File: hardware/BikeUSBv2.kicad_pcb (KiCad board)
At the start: 2 copper layers, 43.6 x 25.5 mm, 53 parts, among them J1 TYPE-C-31-M-16, J2 JST S2B-EH(LF)(SN), SW1 1TS002E-2500-2501-CT, SW2 1TS002E-2500-2501-CT, U1 TPS63020DSJR, U2 ATtiny1616-M, U3 FUSB302B10MPX, U4 HT7550-2, U5 TPS259251

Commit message: remove leftover silkscreen text
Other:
- board text removed: "+ -"
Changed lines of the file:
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@@
     (effects (font (size 1 1) (thickness 0.15)) (justify bottom mirror))
-  )
-  (gr_text "+ -" (at 131 86 90) (layer "B.SilkS")
-    (effects (font (size 1.27 1.27) (thickness 0.15)) (justify top mirror))
   )
   (gr_text "@h3wastooshort\n/BikeUSBv2" (at 153 107) (layer "B.SilkS")

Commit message: slight layout improvment
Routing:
- net /CC_DAC: track 11.0 -> 10.2 mm
- net Net-(JP1-B): track 5.37 -> 4.80 mm

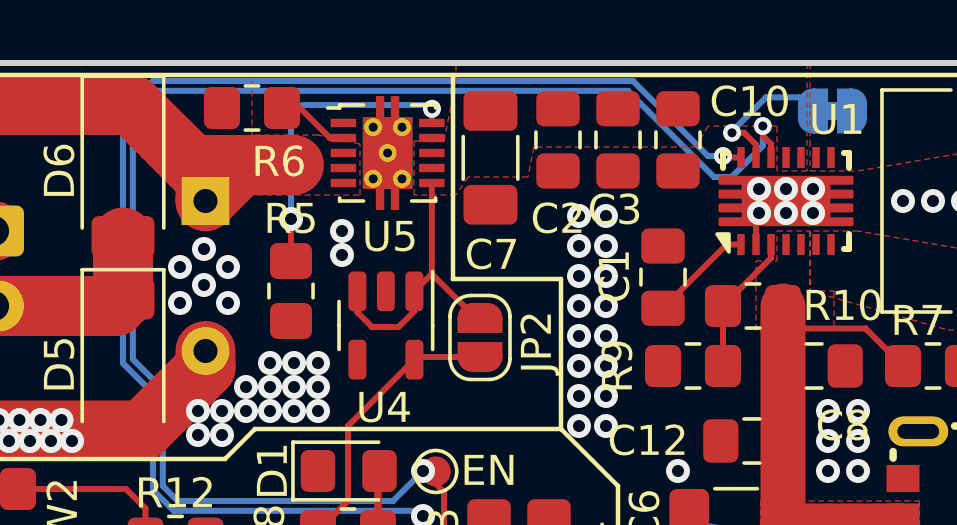
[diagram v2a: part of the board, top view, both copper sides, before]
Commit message: switch eFuse IC in design
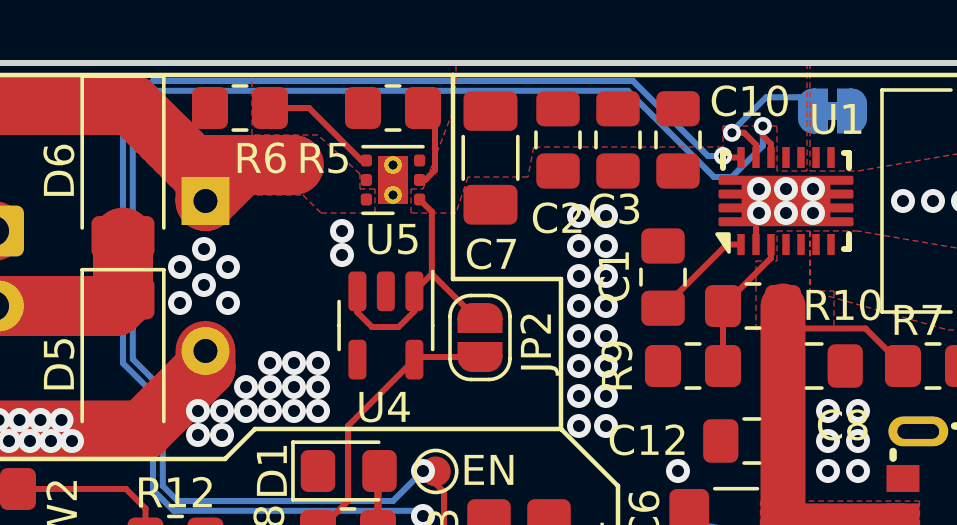
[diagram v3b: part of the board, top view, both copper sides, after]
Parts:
- R5: value 100k -> 33k
- R6: value 1M -> 300k
- U5: value TPS259251 -> TPS25200; footprint Package_SON:VSON-10-1EP_3x3mm_P0.5mm_EP1.65x2.4mm_ThermalVias -> Package_SON:WSON-6-1EP_2x2mm_P0.65mm_EP1x1.6mm_ThermalVias
- moved R5 6.98 mm to (129.5, 83.9), turned to 180 degrees
- moved U5 0.92 mm to (129.5, 86.3), turned to 180 degrees
- moved R6 0.40 mm to (124.4, 83.9)
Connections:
- R6 pad 2: Net-(U5-EN/UVLO) -> Net-(U5-EN)
- U5 pad 1: unconnected-(U5-dV/dT-Pad1) -> +6V
- U5 pad 2: Net-(U5-EN/UVLO) -> Net-(U5-ILIM)
- U5 pad 3: VPP -> unconnected-(U5-FAULT-Pad3)
- U5 pad 4: VPP -> Net-(U5-EN)
- U5 pad 5: VPP -> GND
- U5 pad 6: +6V -> VPP
- U5 pad 7: +6V -> GND
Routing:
- net Net-(U5-ILIM): track 10.2 -> 2.89 mm, vias 2 -> 0
- net Net-(U5-EN): track 0.00 -> 3.54 mm
- net Net-(U5-EN/UVLO): track 2.46 -> 0.00 mm

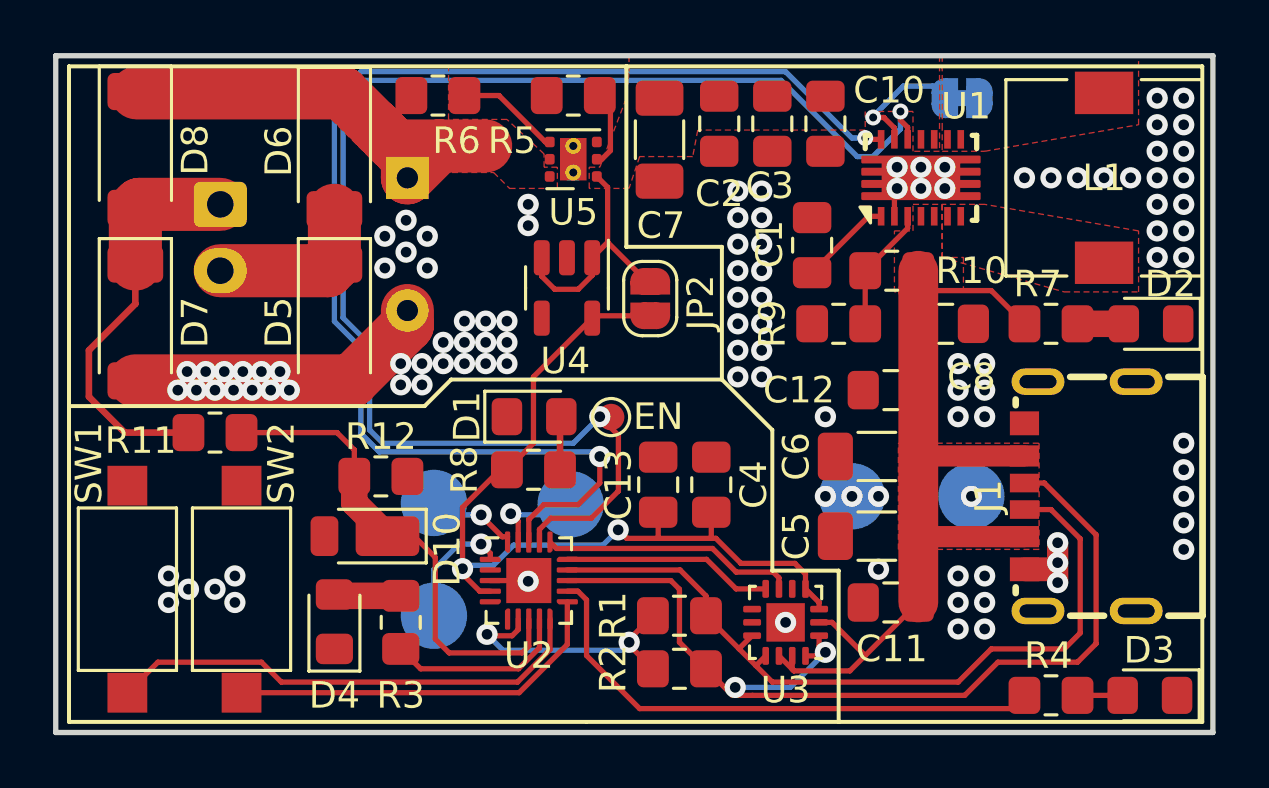
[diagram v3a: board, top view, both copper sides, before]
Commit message: make U4 optional since new U5 clamps to 5V5
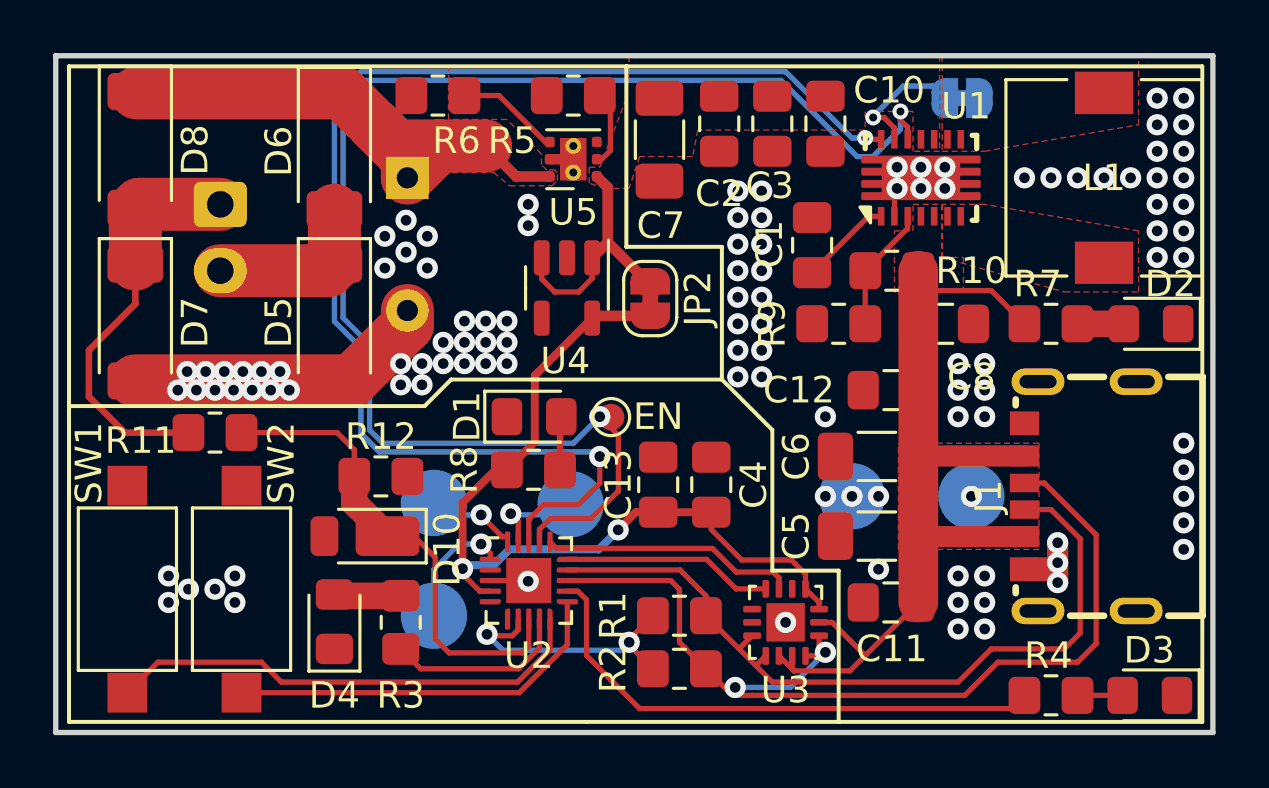
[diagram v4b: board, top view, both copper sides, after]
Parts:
- JP2: footprint Jumper:SolderJumper-2_P1.3mm_Open_RoundedPad1.0x1.5mm -> Jumper:SolderJumper-2_P1.3mm_Bridged_RoundedPad1.0x1.5mm
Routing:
- net VPP: track 18.2 -> 21.1 mm
- net VCC: track 33.1 -> 32.1 mm
- net GND: track 16.7 -> 17.5 mm

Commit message: cleanup
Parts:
- moved C3 1.38 mm to (132.8, 86.9)
- moved R1 0.60 mm to (125.0, 83.9)
- renumbered C9 to C0, C2 to C1, C4 to C10, C5 to C11, C11 to C12, C3 to C2, C7 to C3, C10 to C4, C1 to C5, C8 to C6, C12 to C7, C6 to C8, C13 to C9, JP2 to JP1, JP1 to JP2, R6 to R1, R1 to R10, R2 to R11, R4 to R12, R5 to R2, R10 to R3, R9 to R4, R7 to R5, R11 to R6, R12 to R7, R3 to R9, SW2 to SW1, SW1 to SW2, TP7 to TP1, TP6 to TP2, TP2 to TP3, TP1 to TP4, TP4 to TP5, TP5 to TP6

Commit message: auto cleanup
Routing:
- net Net-(U5-ILIM): track 2.89 -> 2.32 mm
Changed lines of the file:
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@@
   (segment (start 138.7625 103.25) (end 138.7625 103) (width 0.2) (layer "F.Cu") (net 3))
   (segment (start 131.8565 99.6) (end 131.191 100.2655) (width 0.3) (layer "F.Cu") (net 3))
-  (segment (start 130.3 92.2) (end 130.2125 92.2875) (width 0.2) (layer "F.Cu") (net 3))
   (segment (start 138.25 101.928) (end 137.722 101.4) (width 0.2) (layer "F.Cu") (net 3))
   (segment (start 125.975 102.575) (end 125.327 101.927) (width 0.2) (layer "F.Cu") (net 3))
@@
   (segment (start 148.5 105.25) (end 145.5 105.25) (width 0.2) (layer "F.Cu") (net 27))
   (segment (start 149.2 104.55) (end 148.5 105.25) (width 0.2) (layer "F.Cu") (net 27))
-  (segment (start 136.25 106.5) (end 135.5 106.5) (width 0.2) (layer "F.Cu") (net 27))
+  (segment (start 135.5 106.5) (end 144.25 106.5) (width 0.2) (layer "F.Cu") (net 27))
   (segment (start 147.25 98.5) (end 149.2 100.45) (width 0.2) (layer "F.Cu") (net 27))
   (segment (start 149.2 100.45) (end 149.2 104.55) (width 0.2) (layer "F.Cu") (net 27))
   (segment (start 146.5 98.5) (end 147.25 98.5) (width 0.2) (layer "F.Cu") (net 27))
   (segment (start 135.6 106.2) (end 135.6 106.4) (width 0.2) (layer "F.Cu") (net 27))
-  (segment (start 144.25 106.5) (end 136.25 106.5) (width 0.2) (layer "F.Cu") (net 27))
   (segment (start 133.5 102.5) (end 133.175 102.175) (width 0.2) (layer "F.Cu") (net 27))
   (segment (start 138.7625 104.64) (end 139 104.8775) (width 0.2) (layer "F.Cu") (net 27))
@@
   (segment (start 130.795 89.43) (end 130.2125 90.0125) (width 0.4) (layer "F.Cu") (net 36))
   (segment (start 129.7 91.3) (end 128.8 91.3) (width 0.2) (layer "F.Cu") (net 36))
-  (segment (start 132.4 90.9) (end 132.265 90.9) (width 0.4) (layer "F.Cu") (net 36))
   (segment (start 130.3875 86.95) (end 130.795 87.3575) (width 0.4) (layer "F.Cu") (net 36))
   (segment (start 130.2125 90.0125) (end 130.2125 90.7875) (width 0.2) (layer "F.Cu") (net 36))
@@
   (segment (start 130.2125 90.7875) (end 129.7 91.3) (width 0.2) (layer "F.Cu") (net 36))
   (segment (start 128.8 91.3) (end 128.3125 90.8125) (width 0.2) (layer "F.Cu") (net 36))
-  (segment (start 130.9 84.3) (end 130.5 83.9) (width 0.2) (layer "F.Cu") (net 37))
   (segment (start 130.574999 86.3) (end 130.9 85.974999) (width 0.2) (layer "F.Cu") (net 37))
   (segment (start 130.3875 86.3) (end 130.574999 86.3) (width 0.2) (layer "F.Cu") (net 37))
